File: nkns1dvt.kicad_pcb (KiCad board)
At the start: 2 copper layers, 170.7 x 126.8 mm, 79 parts, among them J1 MJ-4PP-9, J2 SERIAL_LED, SW1 SW_RESET, SW10 SW_PUSH, SW11 SW_PUSH, SW12 SW_PUSH, SW13 SW_PUSH, SW14 SW_PUSH, SW15 SW_PUSH, SW16 SW_PUSH, SW17 SW_PUSH, SW18 SW_PUSH, SW19 SW_PUSH, SW2 SW_PUSH, SW20 SW_PUSH, SW21 SW_PUSH, SW22 SW_PUSH, SW23 SW_PUSH, SW24 SW_PUSH, SW25 SW_PUSH, SW26 SW_PUSH, SW27 SW_PUSH, SW28 SW_PUSH, SW29 SW_PUSH, SW3 SW_PUSH, SW30 SW_PUSH, SW31 SW_PUSH, SW32 SW_PUSH, SW33 SW_PUSH, SW34 SW_PUSH, SW4 SW_PUSH, SW5 SW_PUSH, SW6 SW_PUSH, SW7 SW_PUSH, SW8 SW_PUSH, SW9 SW_PUSH, U1 ProMicro

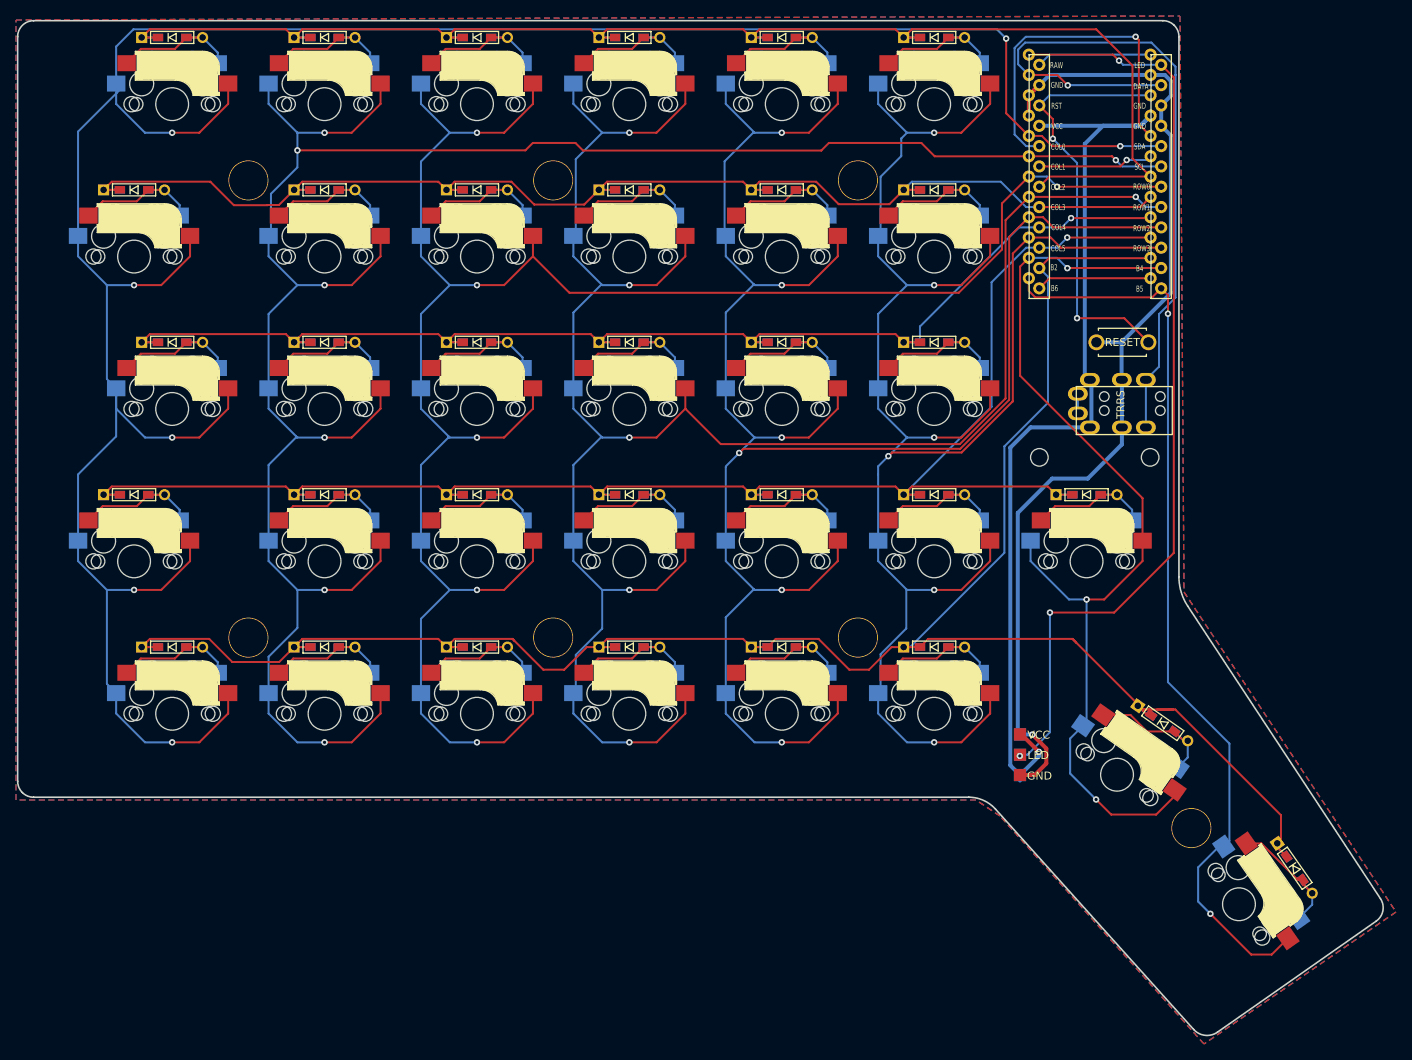
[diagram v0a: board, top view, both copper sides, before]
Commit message: nkns1 rev.0.2
* Change row0-row5 port.
* Add rotary encoder.
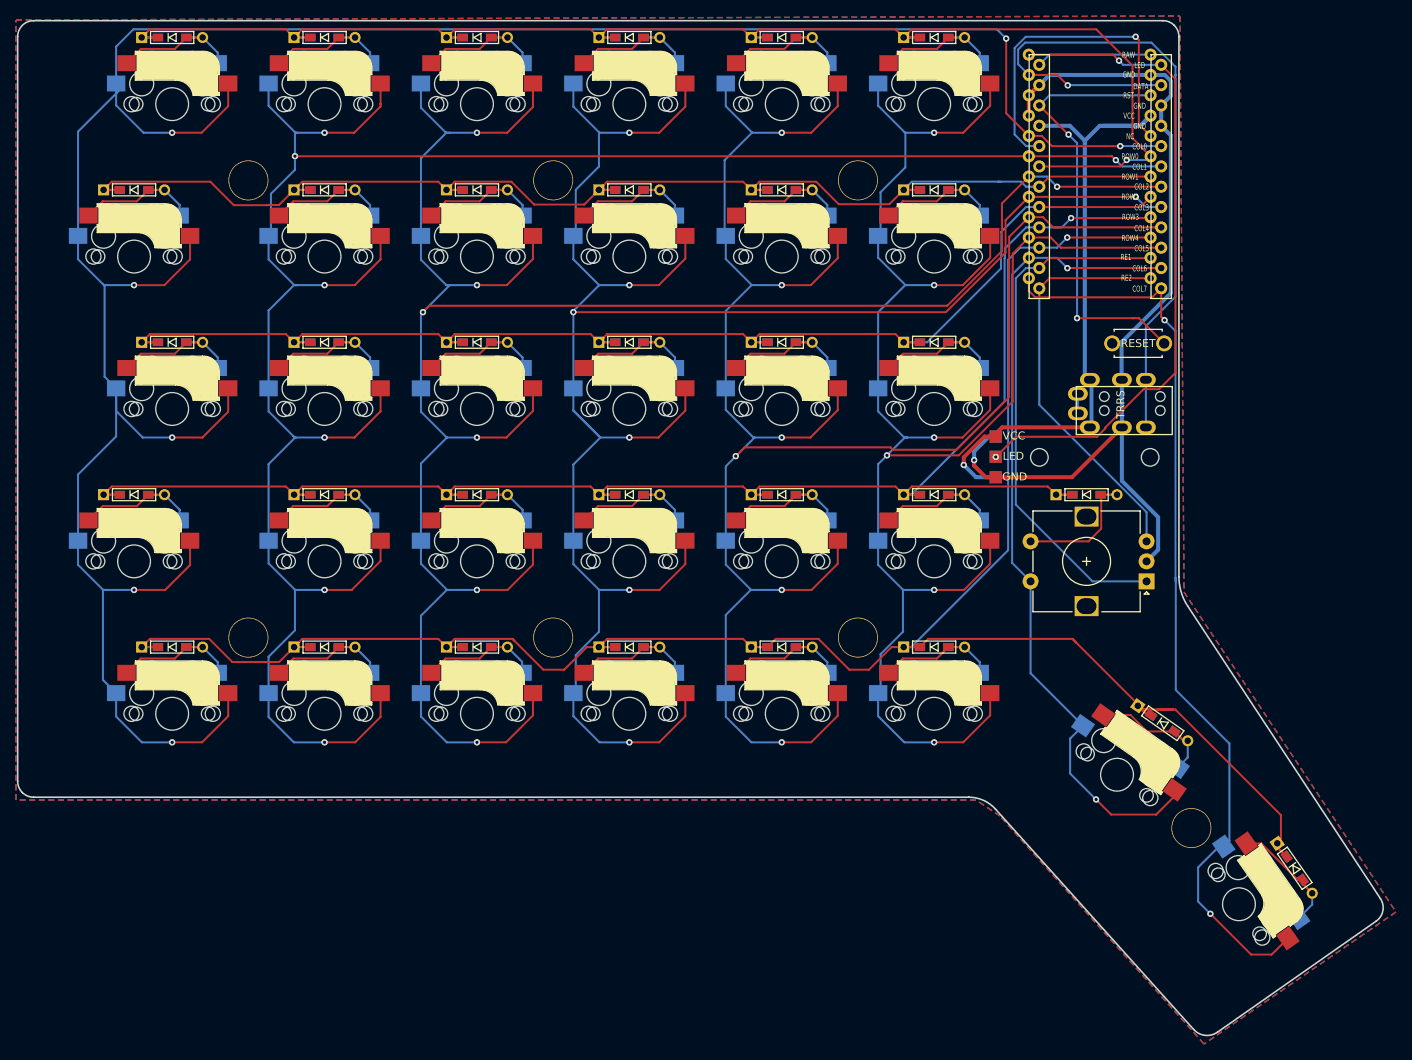
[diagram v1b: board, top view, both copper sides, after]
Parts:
- removed SW26: SW_PUSH, kbd:CherryMX_MidHeight_Hotswap
- added SW35: Rotary_Encoder_Switch, Rotary_Encoder:RotaryEncoder_Alps_EC12E-Switch_Vertical_H20mm, F.Cu at (168.1, 91.3)
- moved J2 37.4 mm to (149.2, 78.3)
- moved SW1 1.97 mm to (167.0, 61.6)
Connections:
- D25 pad 2: Net-(D25-Pad2) -> RE_SW
- U1 pad 13: Net-(U1-Pad13) -> re2
- U1 pad 14: row4 -> re1
- U1 pad 15: row3 -> row4
- U1 pad 16: row2 -> row3
- U1 pad 17: row1 -> row2
- U1 pad 18: row0 -> row1
- U1 pad 19: Net-(U1-Pad19) -> row0
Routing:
- net re1: track 0.00 -> 66.5 mm
- net re2: track 0.00 -> 51.6 mm
- net VCC: track 121.2 -> 82.0 mm
- net led: track 119.0 -> 83.2 mm, vias 3 -> 2
- net Net-(D25-Pad2): track 18.4 -> 0.00 mm
- net RE_SW: track 0.00 -> 17.8 mm
- net col6: track 121.8 -> 104.3 mm, vias 3 -> 2
- net col2: track 258.8 -> 274.2 mm, vias 6 -> 7
- net Net-(U1-Pad13): track 14.4 -> 0.00 mm
- net Net-(U1-Pad19): track 14.4 -> 0.00 mm, vias 1 -> 0
- net GND: track 129.7 -> 117.7 mm
- net row4: track 270.1 -> 273.3 mm, vias 0 -> 1
- net row3: track 206.7 -> 209.8 mm
- net col0: track 327.6 -> 330.7 mm
- net row2: track 160.4 -> 162.9 mm, vias 1 -> 0
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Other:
- board text added: "Ki-1-r0.2 (nkns1) Designed by nekomimist.org"
- board text removed: "Ki-1-r0.1 (nkns1dvt) Designed by nekomimist.org"
